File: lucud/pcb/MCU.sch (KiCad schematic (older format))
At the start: 7 parts, among them U1 STM32F373VCTx

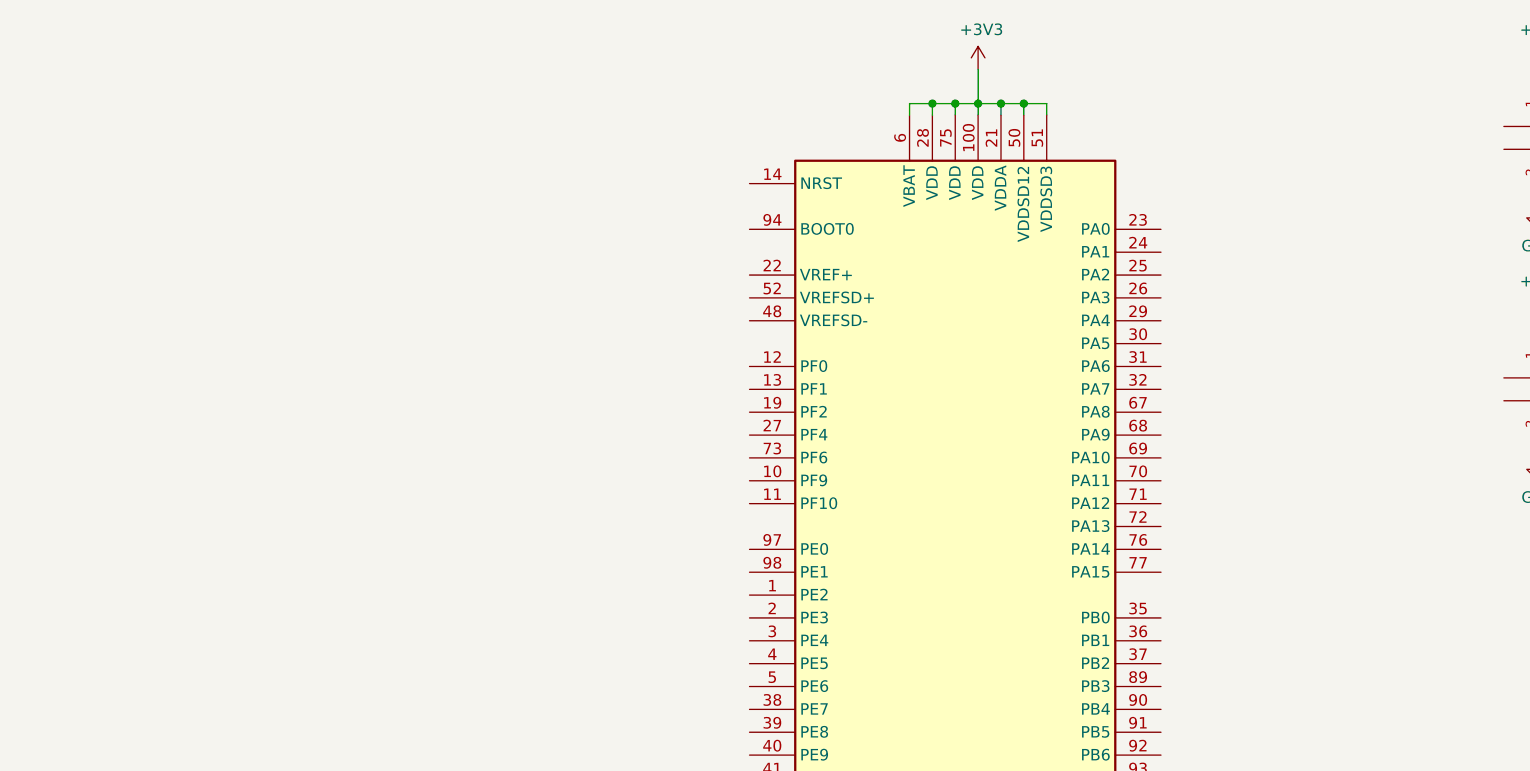
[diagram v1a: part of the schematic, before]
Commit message: Routed some of the lines in.
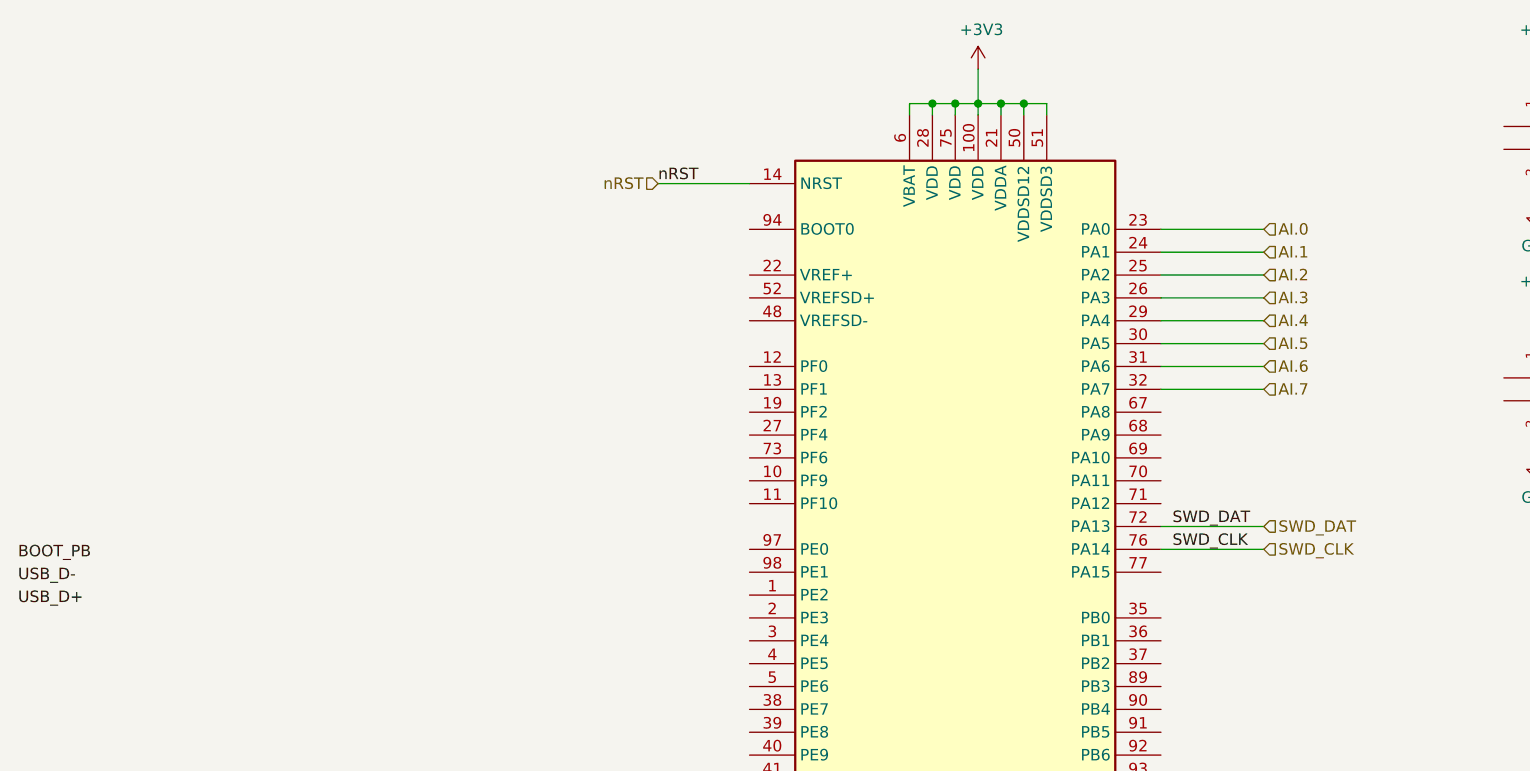
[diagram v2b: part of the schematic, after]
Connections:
- net nRST: now reaches U1.14 (NRST)
- net AI.0: now reaches U1.23 (PA0)
- net AI.1: now reaches U1.24 (PA1)
- net AI.2: now reaches U1.25 (PA2)
- net AI.3: now reaches U1.26 (PA3)
- net AI.4: now reaches U1.29 (PA4)
- net AI.5: now reaches U1.30 (PA5)
- net AI.6: now reaches U1.31 (PA6)
- net AI.7: now reaches U1.32 (PA7)
- net SWD_DAT: now reaches U1.72 (PA13)
- net SWD_CLK: now reaches U1.76 (PA14)
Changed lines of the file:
@@
 Wire Wire Line
 	7450 2850 7450 2800
+Text Label 3600 1650 0    50   ~ 0
+nRST
+Text Label 5850 3250 0    50   ~ 0
+SWD_CLK
+Text Label 5850 3150 0    50   ~ 0
+SWD_DAT
+Text Label 800  3500 0    50   ~ 0
+USB_D+
+Text Label 800  3400 0    50   ~ 0
+USB_D-
+Text Label 800  3300 0    50   ~ 0
+BOOT_PB
+Wire Wire Line
+	5800 3150 6250 3150
+Text HLabel 6250 3150 2    50   Input ~ 0
+SWD_DAT
+Wire Wire Line
+	3600 1650 4000 1650
+Text HLabel 3600 1650 0    50   Input ~ 0
+nRST
+Wire Wire Line
+	5800 3250 6250 3250
+Text HLabel 6250 3250 2    50   Input ~ 0
+SWD_CLK
+Text HLabel 6250 1850 2    50   Input ~ 0
+AI.0
+Text HLabel 6250 1950 2    50   Input ~ 0
+AI.1
+Text HLabel 6250 2050 2    50   Input ~ 0
+AI.2
+Text HLabel 6250 2150 2    50   Input ~ 0
+AI.3
+Text HLabel 6250 2250 2    50   Input ~ 0
+AI.4
+Text HLabel 6250 2350 2    50   Input ~ 0
+AI.5
+Text HLabel 6250 2450 2    50   Input ~ 0
+AI.6
+Text HLabel 6250 2550 2    50   Input ~ 0
+AI.7
+Wire Wire Line
+	6250 1850 5800 1850
+Wire Wire Line
+	6250 1950 5800 1950
+Wire Wire Line
+	5800 2050 6250 2050
+Wire Wire Line
+	6250 2150 5800 2150
+Wire Wire Line
+	5800 2250 6250 2250
+Wire Wire Line
+	6250 2350 5800 2350
+Wire Wire Line
+	5800 2450 6250 2450
+Wire Wire Line
+	6250 2550 5800 2550
 $EndSCHEMATC
